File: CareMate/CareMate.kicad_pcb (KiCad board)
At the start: 2 copper layers, 88.9 x 76.2 mm, 20 parts, among them J1 Barrel_Jack_MountingPin, J2 Conn_01x16, J5 Conn_01x06, U1 L7805, U2 LM386, U4 ESP32-DEVKITC-32D

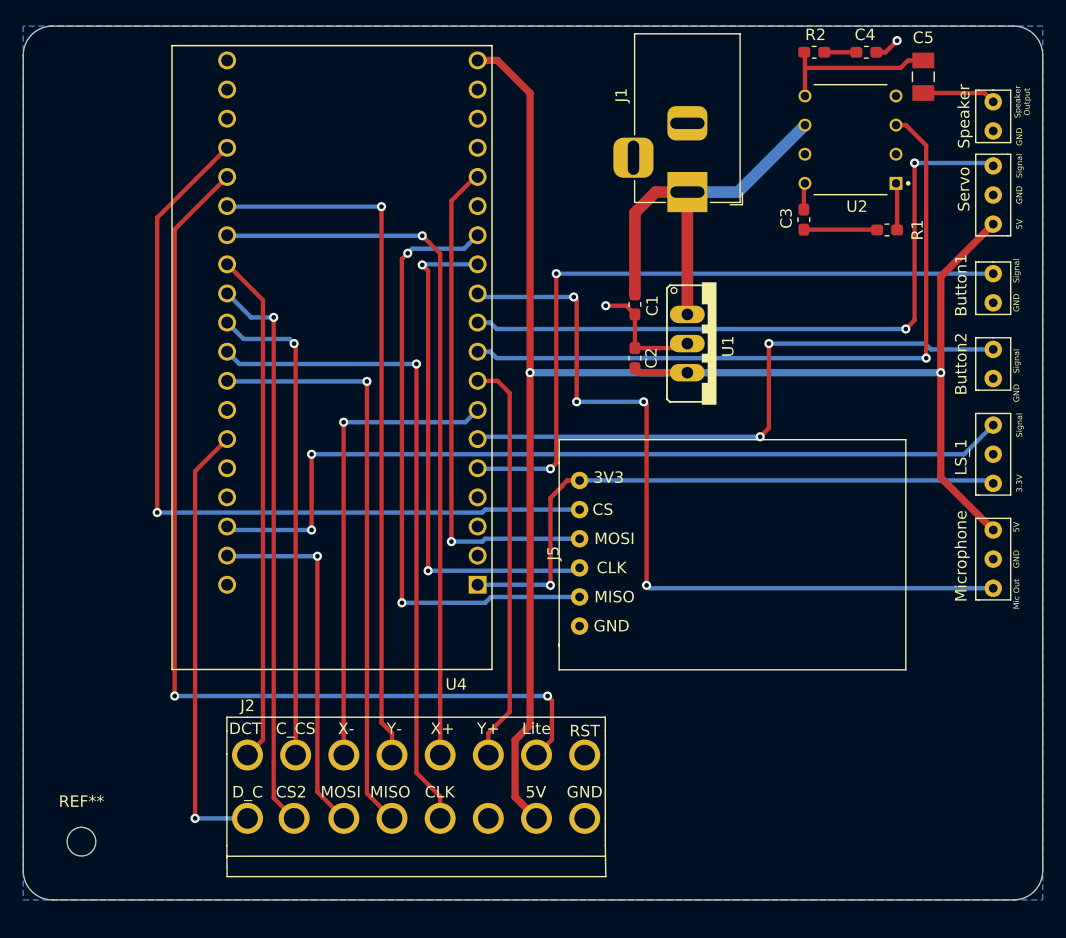
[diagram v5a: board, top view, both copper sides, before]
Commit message: added mounting holes 2.2mm
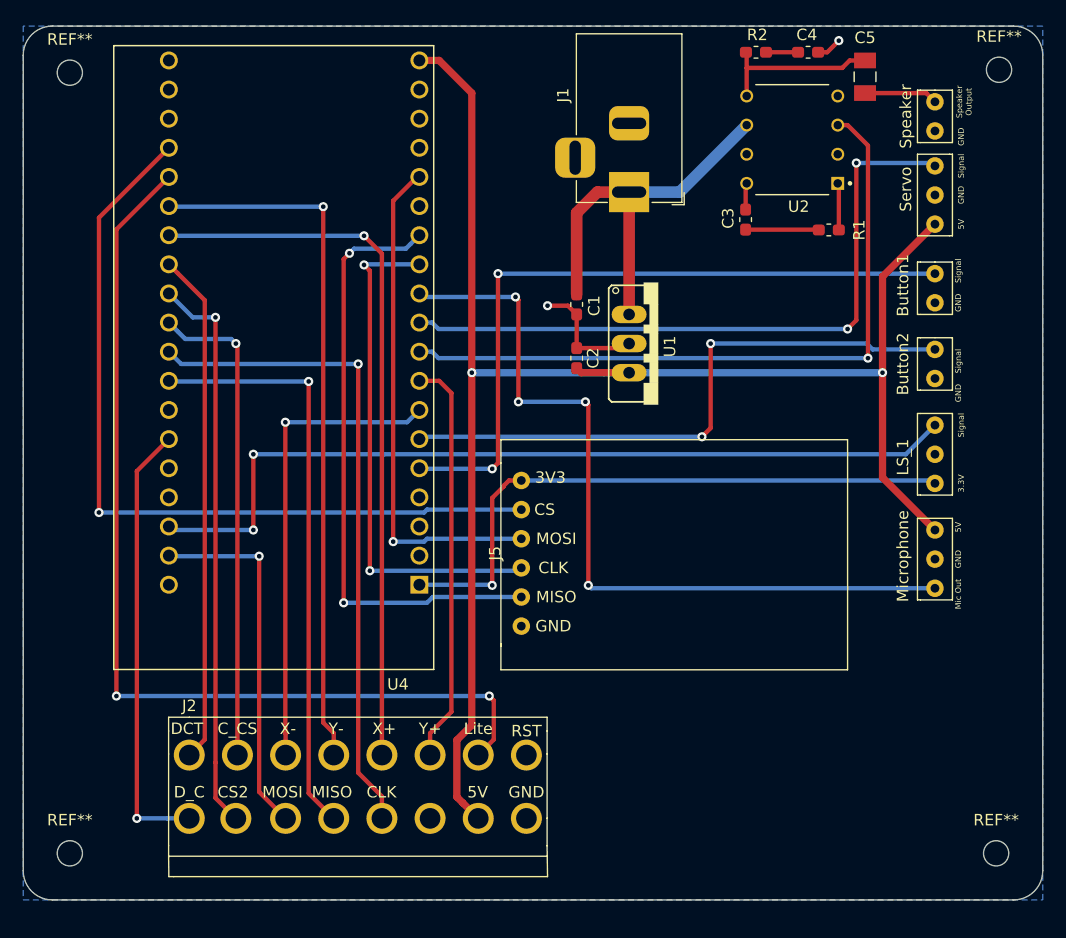
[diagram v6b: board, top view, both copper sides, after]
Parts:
- removed the REF** at (53.3, 96.5)
- added REF**: MountingHole_2.2mm_M2_DIN965, MountingHole:MountingHole_2.2mm_M2_DIN965, F.Cu at (52.3, 29.5)
- added REF**: MountingHole_2.2mm_M2_DIN965, MountingHole:MountingHole_2.2mm_M2_DIN965, F.Cu at (52.3, 97.5)
- added REF**: MountingHole_2.2mm_M2_DIN965, MountingHole:MountingHole_2.2mm_M2_DIN965, F.Cu at (133.3, 29.2)
- added REF**: MountingHole_2.2mm_M2_DIN965, MountingHole:MountingHole_2.2mm_M2_DIN965, F.Cu at (133.1, 97.5)
- moved Button1 5.08 mm to (128.5, 44.7)
- moved Button2 5.08 mm to (128.5, 51.3)
- moved LS_1 5.08 mm to (128.0, 58.2)
- moved Microphone 5.08 mm to (128.0, 67.3)
- moved Speaker 5.08 mm to (128.5, 29.7)
- moved C1 5.08 mm to (96.5, 49.7)
- moved C2 5.08 mm to (96.5, 54.4)
- moved C3 5.08 mm to (111.3, 42.3)
- moved C4 5.08 mm to (116.7, 27.7)
- moved C5 5.08 mm to (121.7, 29.8)
- moved J1 5.08 mm to (101.1, 39.9)
- moved J2 5.08 mm to (62.7, 86.9)
- moved J5 5.08 mm to (91.7, 71.4)
- moved R1 5.08 mm to (118.5, 43.2)
- moved R2 5.08 mm to (112.2, 27.7)
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
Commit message: generated gerbs and step
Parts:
- removed the REF** at (52.3, 29.5)
- removed the REF** at (52.3, 97.5)
- removed the REF** at (133.3, 29.2)
- removed the REF** at (133.1, 97.5)
- added G***: LOGO, Additional Libraries:cyclone, F.Cu at (113.0, 50.0)
- added G***: LOGO, Additional Libraries:cheese, F.Cu at (90.7, 34.5)
- added G***: LOGO, Additional Libraries:carmex, F.Cu at (51.8, 51.3)
- added G***: LOGO, Additional Libraries:discgolf, F.Cu at (53.1, 91.9)
- added G***: LOGO, Additional Libraries:lifealertlady, F.Cu at (108.0, 71.9)
- added REF**: MountingHole_2.2mm_M2_DIN965, MountingHole:MountingHole_2.2mm_M2_DIN965, F.Cu at (52.6, 29.7)
- added REF**: MountingHole_2.2mm_M2_DIN965, MountingHole:MountingHole_2.2mm_M2_DIN965, F.Cu at (132.8, 29.7)
- added REF**: MountingHole_2.2mm_M2_DIN965, MountingHole:MountingHole_2.2mm_M2_DIN965, F.Cu at (132.8, 97.3)
- added REF**: MountingHole_2.2mm_M2_DIN965, MountingHole:MountingHole_2.2mm_M2_DIN965, F.Cu at (52.1, 97.8)
- renumbered Button1 to Button_1, Button2 to Button_2, U4 to U3
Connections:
- J2 pad 16: Card_Detect -> Net-(J2-Pad16)
- J2 pad 9: Net-(J2-Pad9) -> RST
- U3 pad 31: Card_Detect -> RST
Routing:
- net RST: track 0.00 -> 72.4 mm, vias 0 -> 2
- net Card_Detect: track 44.6 -> 0.00 mm
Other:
- board text added: "[CAREMATE REV 2] [Senior Design 2] [Labbloe Jonnor Jared Jack]"
- board text removed: "CAREMATE REV 1 Senior Design 2"
